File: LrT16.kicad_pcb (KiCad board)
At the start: 4 copper layers, 100 x 100 mm, 160 parts, among them J1 USB_C_Receptacle_USB2.0, J2 Conn_02x07_Odd_Even, Q1 2N7002, Q2 2N7002, SW0 EC11_SMD, SW1 EC11_SMD, SW10 EC11_SMD, SW11 EC11_SMD, SW12 EC11_SMD, SW13 EC11_SMD, SW14 EC11_SMD, SW15 EC11_SMD, SW17 SW_Push, SW18 SW_Push, SW19 SW_SPST, SW2 EC11_SMD, SW3 EC11_SMD, SW4 EC11_SMD, SW5 EC11_SMD, SW6 EC11_SMD, SW7 EC11_SMD, SW8 EC11_SMD, SW9 EC11_SMD, U1 STM32F072R8Tx, U2 SPX3819M5-L3-3TR

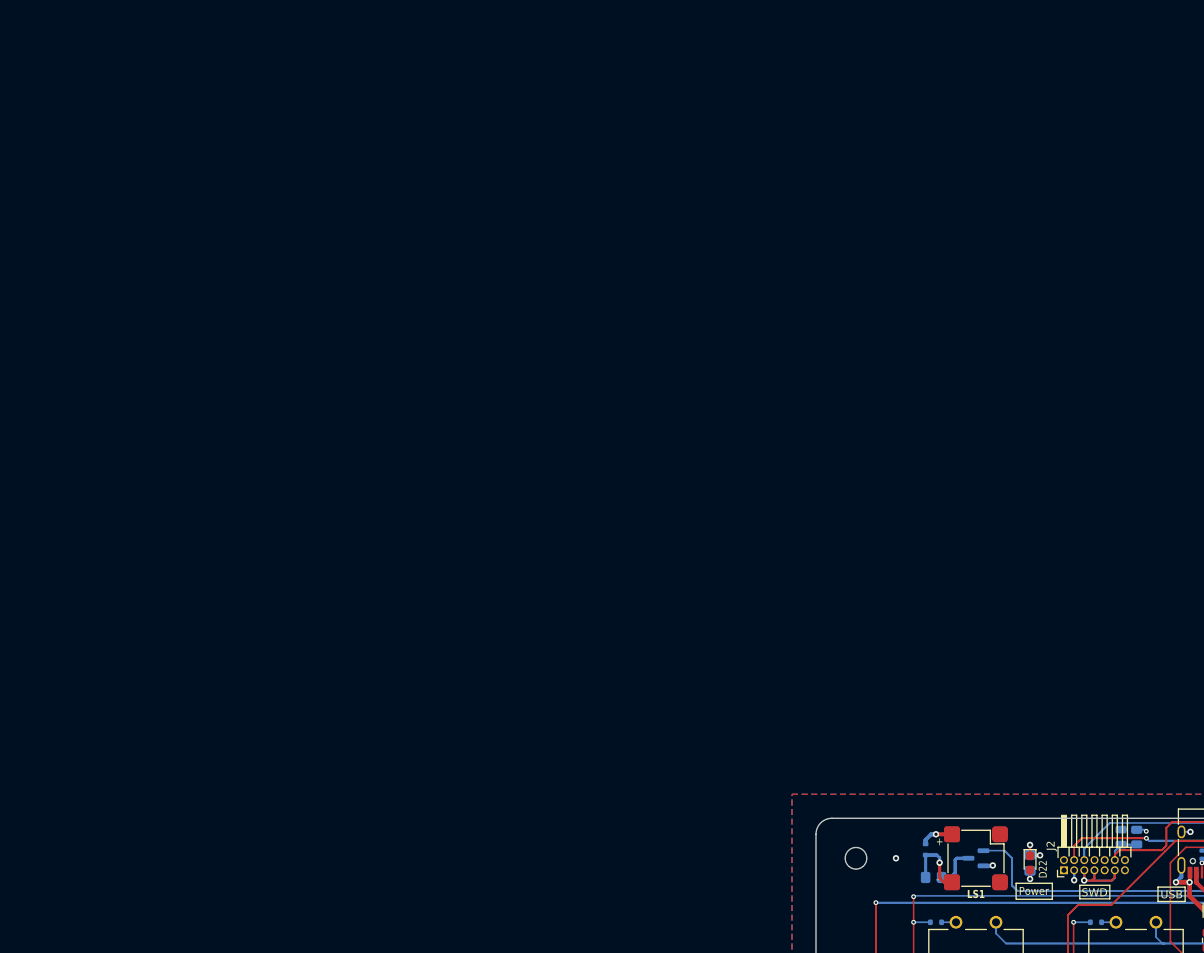
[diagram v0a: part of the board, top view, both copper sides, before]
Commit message: mod. J2 footprint
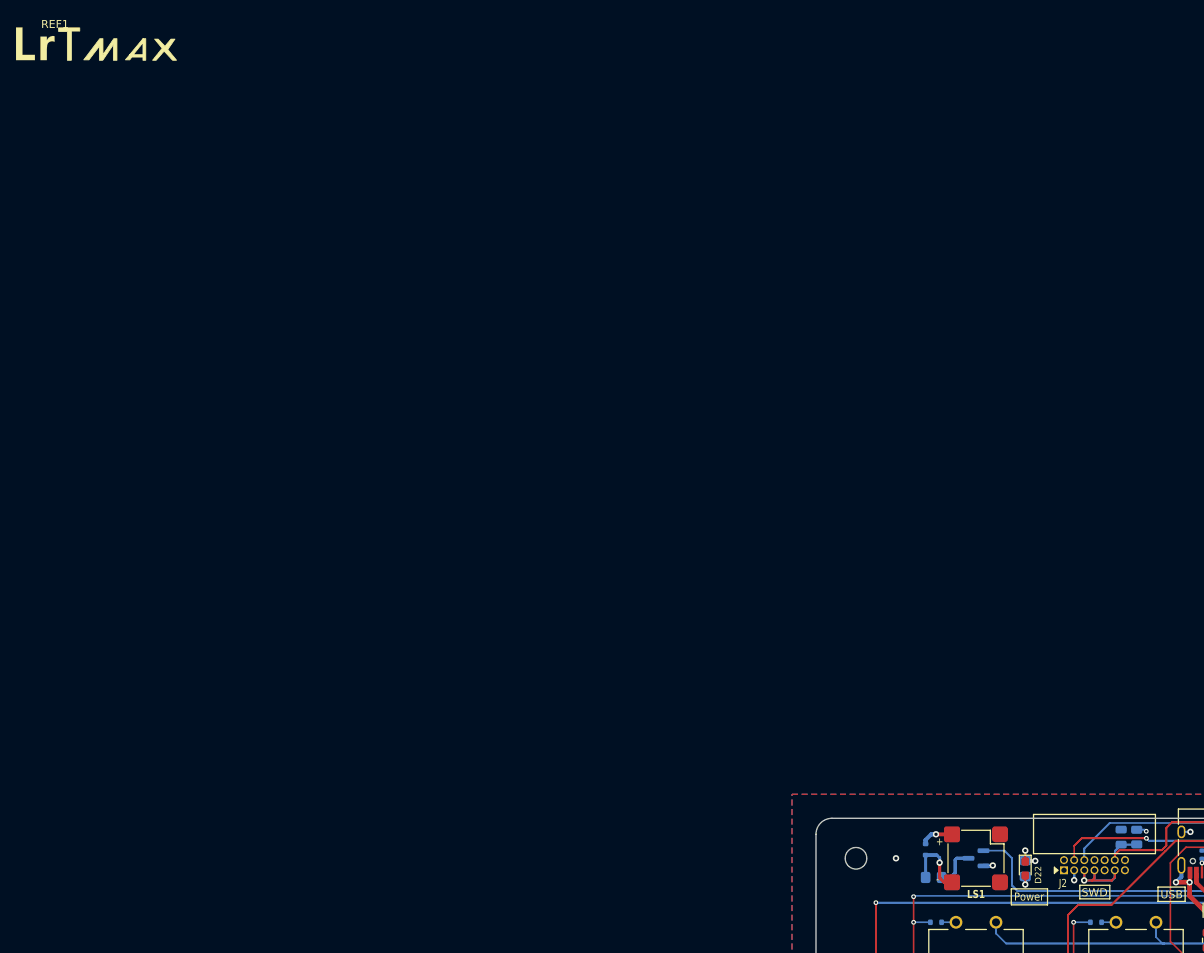
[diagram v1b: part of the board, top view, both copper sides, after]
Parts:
- added REF1: LRTMAX-LOGO, LrE-6:LrTMAX-LOGO, F.Cu at (4.87, 0.25)
- moved D22 0.92 mm to (126.2, 106.3)
- moved R37 0.92 mm to (126.2, 106.3)
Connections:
- U1 pad 8: /E1A -> /E0A
- U1 pad 9: /E1B -> /E0B

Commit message: working on LrT16.pb
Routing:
- net /E0A: track 5.77 -> 167.2 mm, vias 0 -> 2
- net /NRST: track 98.9 -> 69.8 mm
- net /L3: track 145.4 -> 125.5 mm
- net /M2: track 117.4 -> 98.9 mm
- net /E6A: track 104.3 -> 95.2 mm
- net /E10A: track 3.58 -> 7.32 mm, vias 0 -> 1
- net /E11A: track 4.23 -> 7.86 mm, vias 0 -> 1
- net /E10B: track 3.65 -> 7.26 mm, vias 0 -> 1
- net +3V3: track 73.9 -> 71.4 mm
- net /E9B: track 130.4 -> 129.0 mm

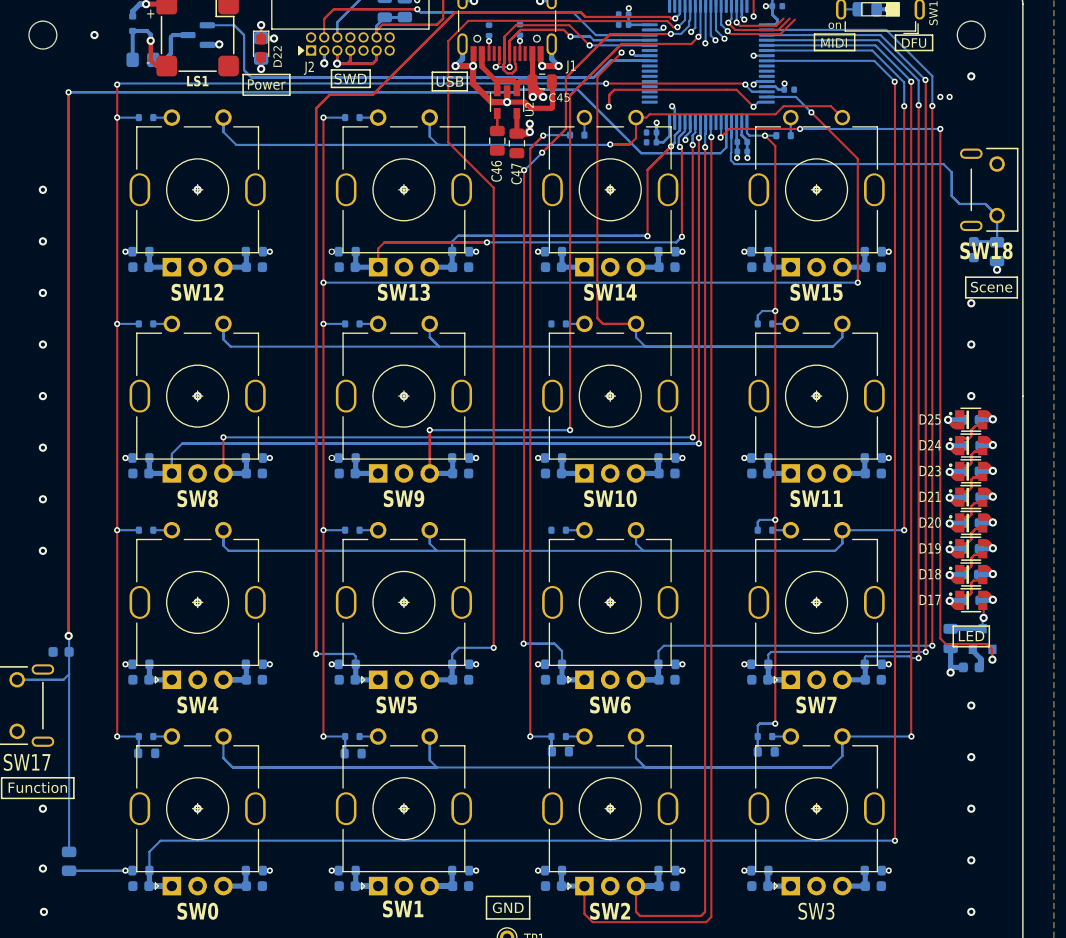
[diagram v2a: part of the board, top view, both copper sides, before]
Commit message: reduce 3.3v fill area
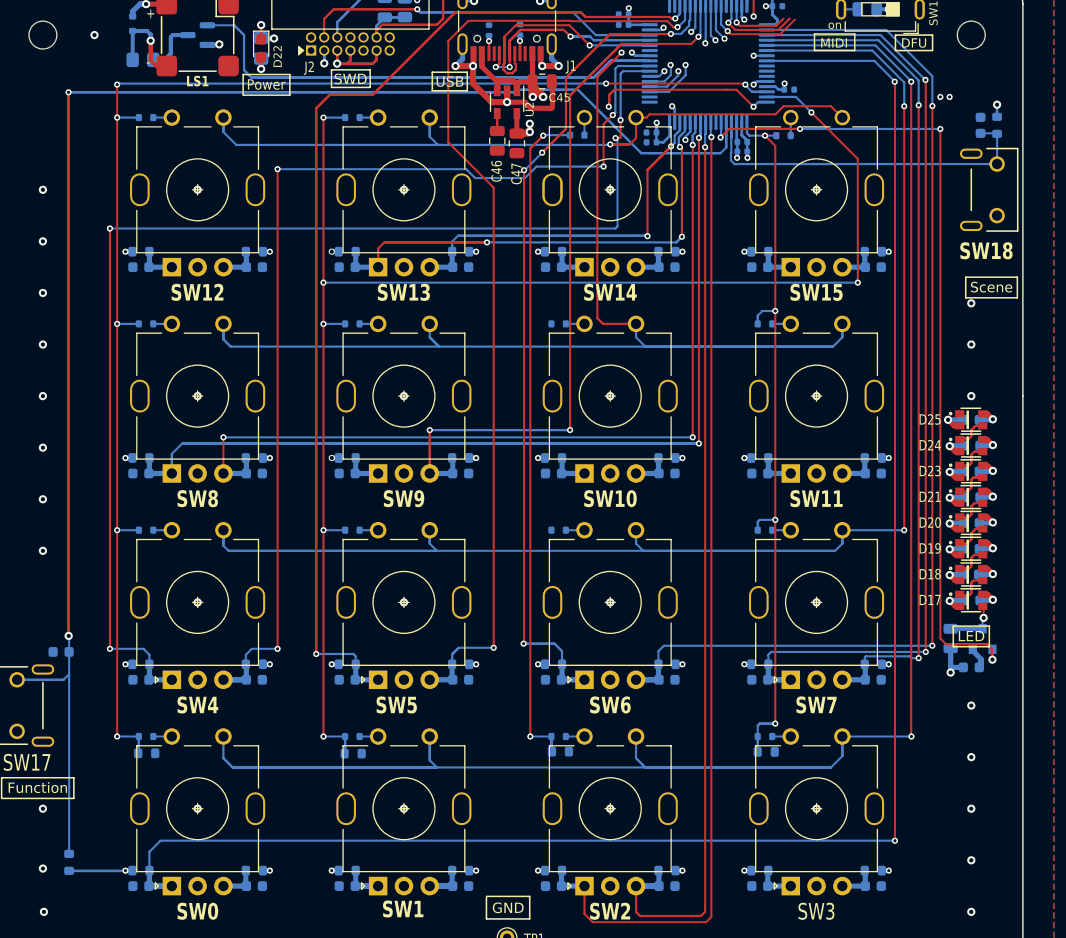
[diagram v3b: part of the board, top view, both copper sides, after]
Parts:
- R39, R40: footprint Resistor_SMD:R_0805_2012Metric -> Resistor_SMD:R_0603_1608Metric
- moved R39 12.2 mm to (197.5, 113.8), turned to -90 degrees
- moved C57 12.1 mm to (195.9, 113.8), turned to 90 degrees
- moved R40 0.10 mm to (107.5, 185.2)
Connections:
- SW18 pad 1: GND -> /SW18
- SW18 pad 2: /SW18 -> GND
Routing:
- net /E4A: track 3.75 -> 117.0 mm, vias 0 -> 4
- net /E4B: track 5.67 -> 102.2 mm, vias 0 -> 4
- net +3V3: track 71.4 -> 99.5 mm
- net /SW18: track 72.2 -> 55.9 mm
- net /E15A: track 3.68 -> 8.82 mm, vias 0 -> 1
- net /E15B: track 3.65 -> 7.28 mm, vias 0 -> 1
- net /E3A: track 3.68 -> 6.97 mm, vias 0 -> 1
- net /E3B: track 3.68 -> 5.31 mm, vias 0 -> 1
- net GND: track 85.8 -> 85.9 mm, vias 72 -> 71

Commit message: fix sylk error
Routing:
- net /E0B: track 3.78 -> 131.7 mm, vias 0 -> 3
- net /E1A: track 5.75 -> 123.7 mm, vias 0 -> 3
- net /E1B: track 5.75 -> 112.5 mm, vias 0 -> 3
- net /E3B: track 5.31 -> 102.7 mm, vias 1 -> 4
- net /E12B: track 10.3 -> 105.7 mm, vias 1 -> 4
- net /E12A: track 12.2 -> 105.9 mm, vias 1 -> 3
- net /E3A: track 6.97 -> 94.8 mm, vias 1 -> 2
- net /E9A: track 8.14 -> 74.3 mm, vias 1 -> 3
- net /E11A: track 7.86 -> 64.3 mm
- net /E11B: track 13.6 -> 60.3 mm, vias 1 -> 3
- net /SWDIO: track 64.6 -> 39.8 mm
- net /E10A: track 7.32 -> 19.0 mm, vias 1 -> 2
- net /E10B: track 7.26 -> 16.6 mm, vias 1 -> 2
- net /M1: track 149.6 -> 145.7 mm
- net /L3: track 125.5 -> 123.7 mm
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
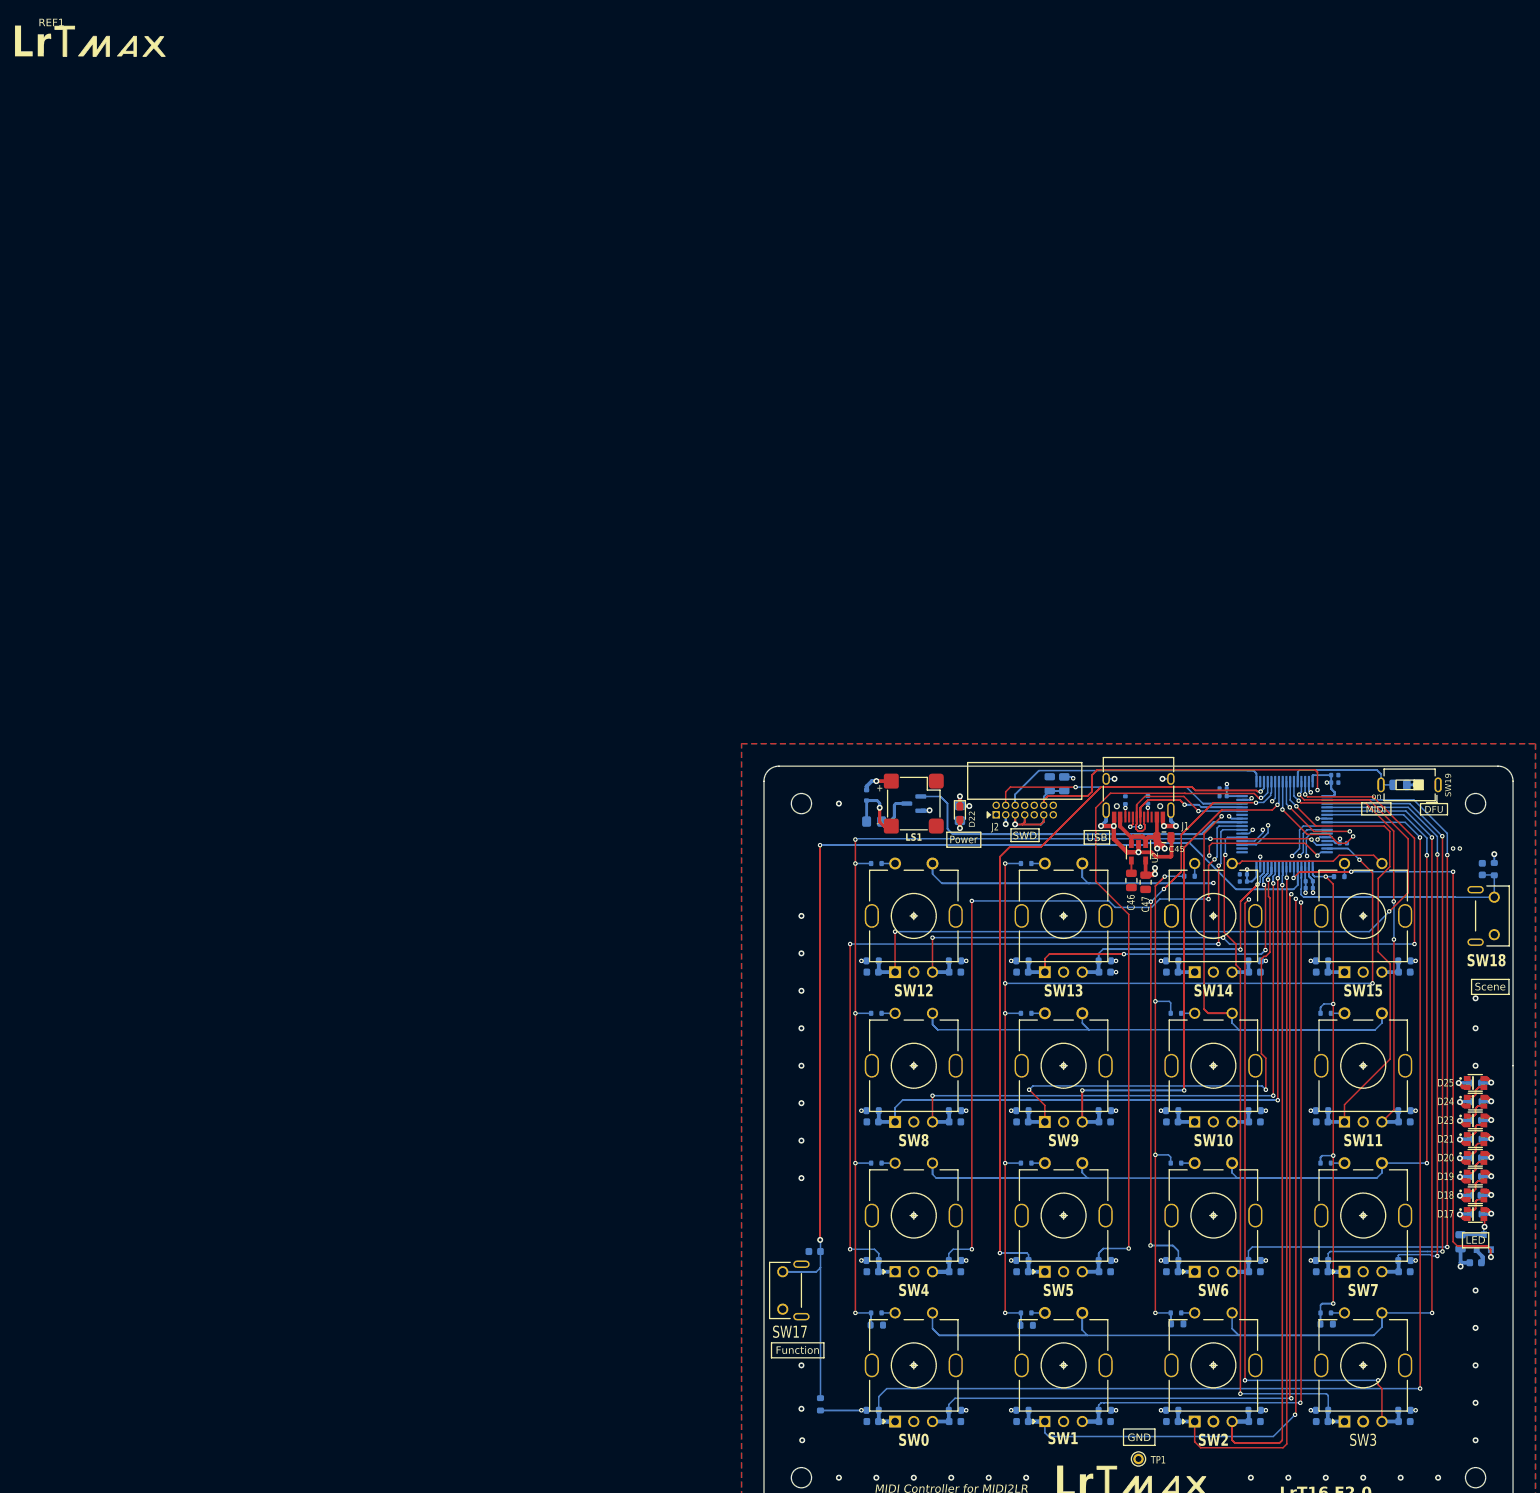
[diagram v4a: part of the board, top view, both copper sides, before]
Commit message: eliminate errors and warnings
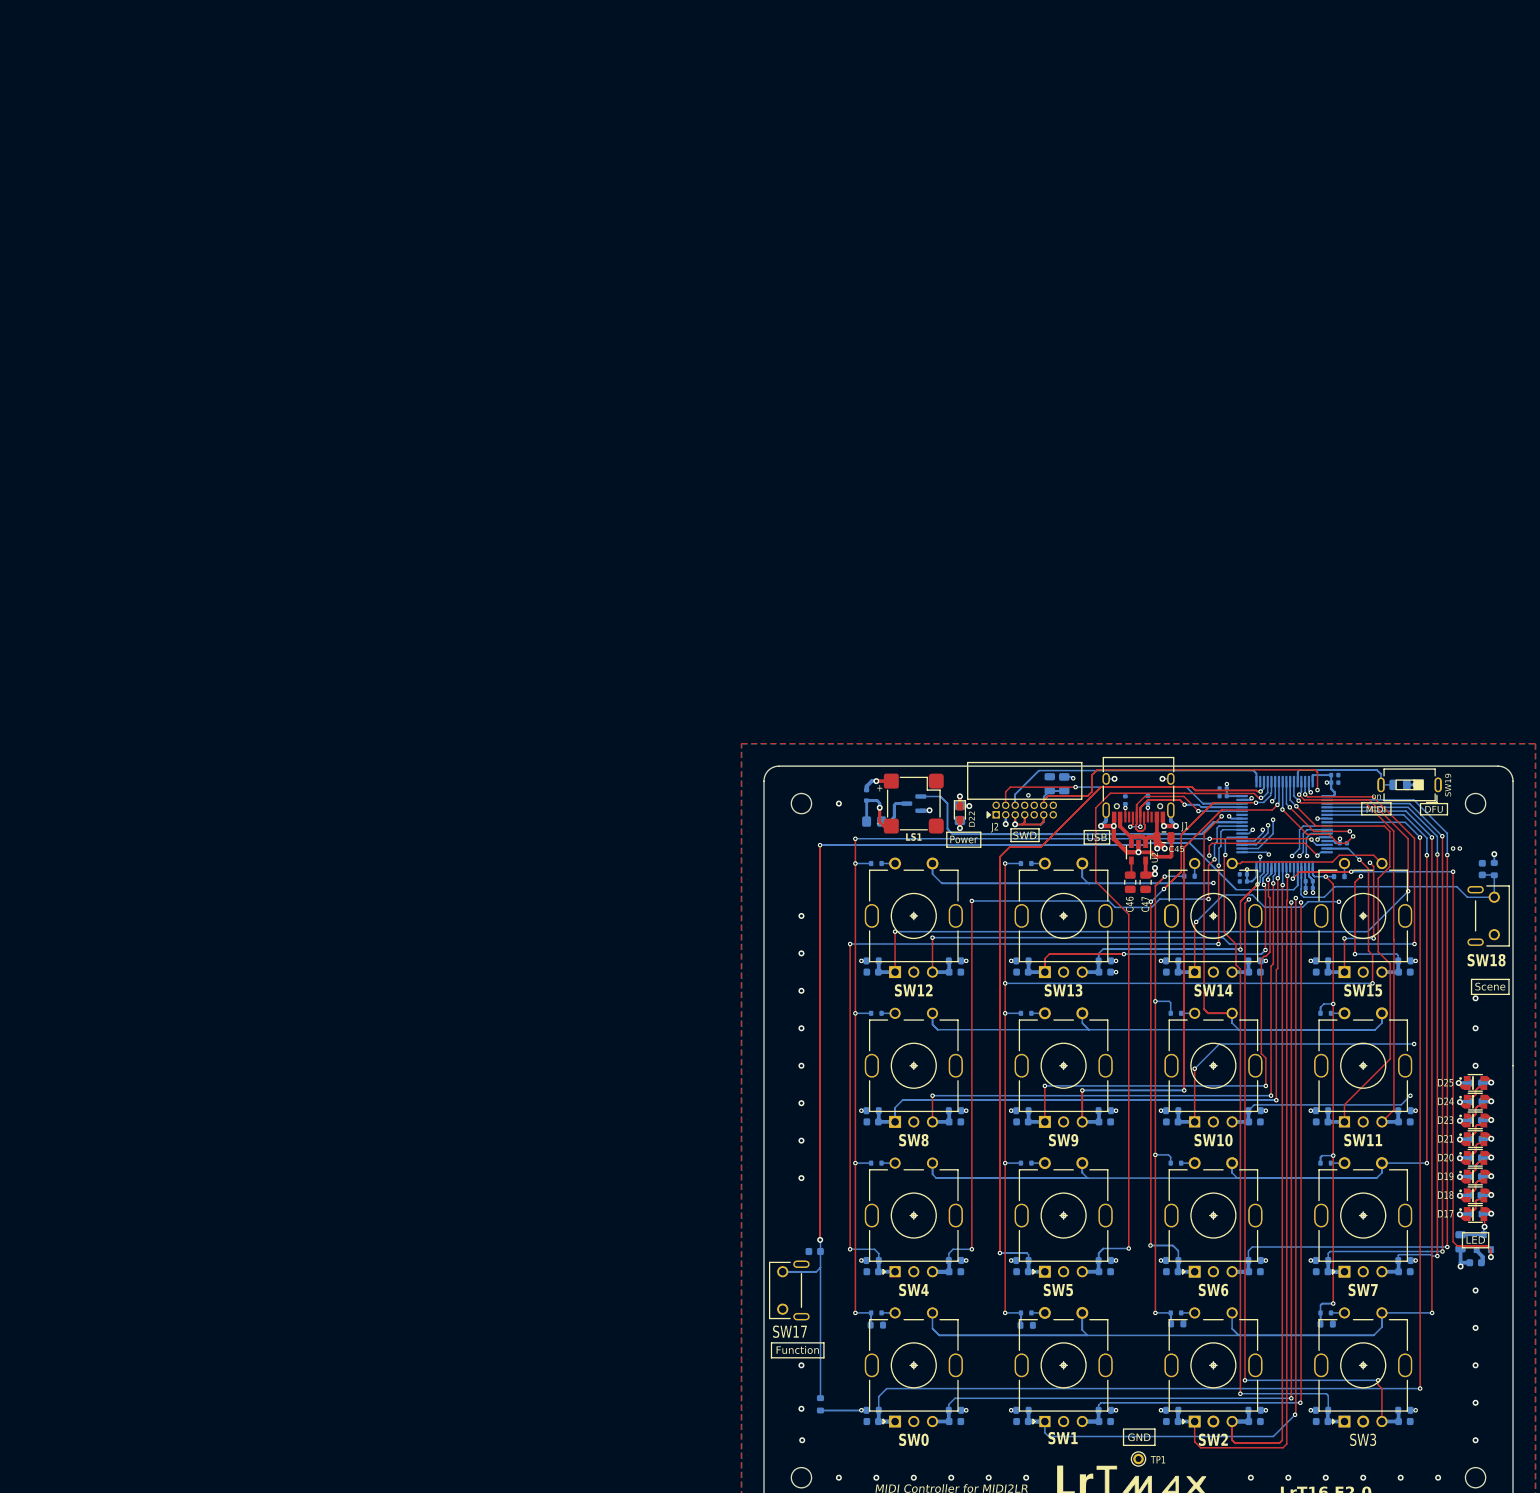
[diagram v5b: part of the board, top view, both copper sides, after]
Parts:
- removed REF1: LRTMAX-LOGO, LrE-6:LrTMAX-LOGO
- moved C46 0.29 mm to (148.9, 115.5)
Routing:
- net /E10A: track 19.0 -> 93.0 mm, vias 2 -> 4
- net /E10B: track 16.6 -> 89.6 mm, vias 2 -> 3
- net /E14A: track 3.65 -> 51.3 mm, vias 0 -> 3
- net /E15A: track 8.82 -> 43.4 mm, vias 1 -> 4
- net /E15B: track 7.28 -> 40.8 mm, vias 1 -> 3
- net /E14B: track 3.65 -> 34.6 mm, vias 0 -> 1
- net /SW18: track 55.9 -> 36.8 mm
- net /SW17: track 273.9 -> 266.3 mm
- net /E9A: track 74.3 -> 70.3 mm
- net /E2B: track 102.5 -> 101.3 mm
- net /E8B: track 84.0 -> 83.1 mm
- net /SWCLK: track 44.7 -> 43.8 mm
- net /E13A: track 61.2 -> 60.4 mm
- net /E13B: track 60.8 -> 60.1 mm
- net GND: vias 72 -> 73
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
